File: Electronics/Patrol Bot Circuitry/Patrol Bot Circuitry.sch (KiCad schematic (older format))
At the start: 40 parts, among them J1 Left_Motor, J2 Right_Motor, J3 Battery, J4 AC_DC_10V, J5 Servo Motor, Q1 IRF4905, Q2 IRF4905, Q3 IRF4905, Q4 IRLZ44N, U1 ROB-14450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

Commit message: CAD Upload 1
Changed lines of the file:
@@
 U 1 1 619EC2A4
 P 3450 2100
-F 0 "U3" H 3650 1800 50  0000 C CNN
+F 0 "U3" H 3700 1800 50  0000 C CNN
 F 1 "MP1584EN" H 3400 1800 50  0000 C CNN
 F 2 "MP1584EN:MP1584EN" H 3450 2100 50  0001 C CNN

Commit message: Software Upload 1
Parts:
- removed C1: 0.1u, Capacitor_THT:CP_Axial_L10.0mm_D4.5mm_P15.00mm_Horizontal, symbol Device:C
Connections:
- net 3.3V: now also U1.2 (VCC)
- net 5V: no longer U1.2 (VCC)
- net IO1: now also U1.13 (STBY); no longer U11.8 (INT)
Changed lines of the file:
@@
-	1    0    0    -1
-$EndComp
-$Comp
-L HC-SR04:HC-SR04 U8
-U 1 1 61A3787B
-P 8300 4000
-F 0 "U8" H 8300 4200 50  0000 L CNN
-F 1 "HC-SR04" H 8450 4200 50  0000 L CNN
-F 2 "Connector_PinHeader_2.54mm:PinHeader_1x04_P2.54mm_Vertical" H 8300 4000 50  0001 L BNN
-F 3 "" H 8300 4000 50  0001 L BNN
-F 4 "Osepp" H 8300 4000 50  0001 L BNN "MANUFACTURER"
-	1    8300 4000
 	1    0    0    -1
 $EndComp
@@
 Wire Wire Line
 	5150 4150 5150 4250
-$Comp
-L Device:D_Photo D1
-U 1 1 61A649FF
-P 1450 6750
-F 0 "D1" V 1450 7050 50  0000 C CNN
-F 1 "D_Photo" V 1350 7050 50  0000 C CNN
-F 2 "OptoDevice:R_LDR_4.9x4.2mm_P2.54mm_Vertical" H 1400 6750 50  0001 C CNN
-F 3 "~" H 1400 6750 50  0001 C CNN
-	1    1450 6750
-	0    -1   -1   0
-$EndComp
 Text Notes 2000 7550 0    50   ~ 0
 Connect ADDR to \nGND for address 0x48.
@@
 	-1   0    0    -1
 $EndComp
-NoConn ~ 2700 4000
 $Comp
 L Connector:Screw_Terminal_01x02 J1
@@
 Wire Wire Line
 	6350 3350 6500 3350
-Wire Wire Line
-	6500 3350 6500 3900
-Wire Wire Line
-	6500 3900 8100 3900
 Wire Wire Line
 	6550 4100 8100 4100
@@
 Text Label 4450 4250 0    50   ~ 0
 IO1
-Text Label 9450 1700 0    50   ~ 0
-IO1
 Text Notes 8350 3100 0    50   ~ 0
 Must initialize IO1 \npin as interrupt.\n
@@
 Wire Wire Line
 	4050 6150 4200 6150
-$Comp
-L Device:C C1
-U 1 1 61C1ABD0
-P 1050 7100
-F 0 "C1" H 850 7100 50  0000 L CNN
-F 1 "0.1u" H 850 7000 50  0000 L CNN
-F 2 "Capacitor_THT:CP_Axial_L10.0mm_D4.5mm_P15.00mm_Horizontal" H 1088 6950 50  0001 C CNN
-F 3 "~" H 1050 7100 50  0001 C CNN
-	1    1050 7100
-	1    0    0    -1
-$EndComp
-Wire Wire Line
-	1050 6950 1450 6950
-Wire Wire Line
-	1050 7250 1450 7250
 NoConn ~ 4450 4050
 Wire Wire Line
@@
 Text Label 4850 6150 0    50   ~ 0
 3.3V
-Text Label 1450 6600 2    50   ~ 0
-3.3V
-Wire Wire Line
-	1450 6650 1450 6600
 Text Label 5950 2000 0    50   ~ 0
 5V
-Text Label 1500 3750 2    50   ~ 0
-5V
 Text Label 3250 3650 2    50   ~ 0
-5V
-Text Label 6500 3350 2    50   ~ 0
 5V
 Text Label 8100 4550 2    50   ~ 0
@@
 Battery
 NoConn ~ 3250 3750
+$Comp
+L HC-SR04:HC-SR04 U8
+U 1 1 61A3787B
+P 8300 4000
+F 0 "U8" H 8300 4200 50  0000 L CNN
+F 1 "HC-SR04" H 8450 4200 50  0000 L CNN
+F 2 "Connector_PinHeader_2.54mm:PinHeader_1x04_P2.54mm_Vertical" H 8300 4000 50  0001 L BNN
+F 3 "" H 8300 4000 50  0001 L BNN
+F 4 "Osepp" H 8300 4000 50  0001 L BNN "MANUFACTURER"
+	1    8300 4000
+	1    0    0    -1
+$EndComp
+Text Label 1500 3750 2    50   ~ 0
+3.3V
+NoConn ~ 9450 1700
+Text Label 2700 4000 0    50   ~ 0
+IO1
+Text Label 6500 3350 2    50   ~ 0
+5V
+Wire Wire Line
+	6500 3350 6500 3900
+Wire Wire Line
+	6500 3900 8100 3900
+Wire Wire Line
+	1450 6650 1450 6600
+Text Label 1450 6600 2    50   ~ 0
+3.3V
+$Comp
+L Device:D_Photo D1
+U 1 1 61A649FF
+P 1450 6750
+F 0 "D1" V 1500 6700 50  0000 C CNN
+F 1 "D_Photo" V 1500 7050 50  0000 C CNN
+F 2 "OptoDevice:R_LDR_4.9x4.2mm_P2.54mm_Vertical" H 1400 6750 50  0001 C CNN
+F 3 "~" H 1400 6750 50  0001 C CNN
+	1    1450 6750
+	0    -1   -1   0
+$EndComp
 $EndSCHEMATC

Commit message: Validation 1
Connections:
- net GND: now also U11.7 (AD0)
- no-connect marks 29 -> 28
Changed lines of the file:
@@
 NoConn ~ 8250 2500
 NoConn ~ 8250 2000
-NoConn ~ 8250 1700
 NoConn ~ 8250 1600
 NoConn ~ 8250 1500
@@
 	0    -1   -1   0
 $EndComp
+$Comp
+L power:GND #PWR?
+U 1 1 61CAC55A
+P 8250 1700
+F 0 "#PWR?" H 8250 1450 50  0001 C CNN
+F 1 "GND" H 8255 1527 50  0000 C CNN
+F 2 "" H 8250 1700 50  0001 C CNN
+F 3 "" H 8250 1700 50  0001 C CNN
+	1    8250 1700
+	1    0    0    -1
+$EndComp
 $EndSCHEMATC

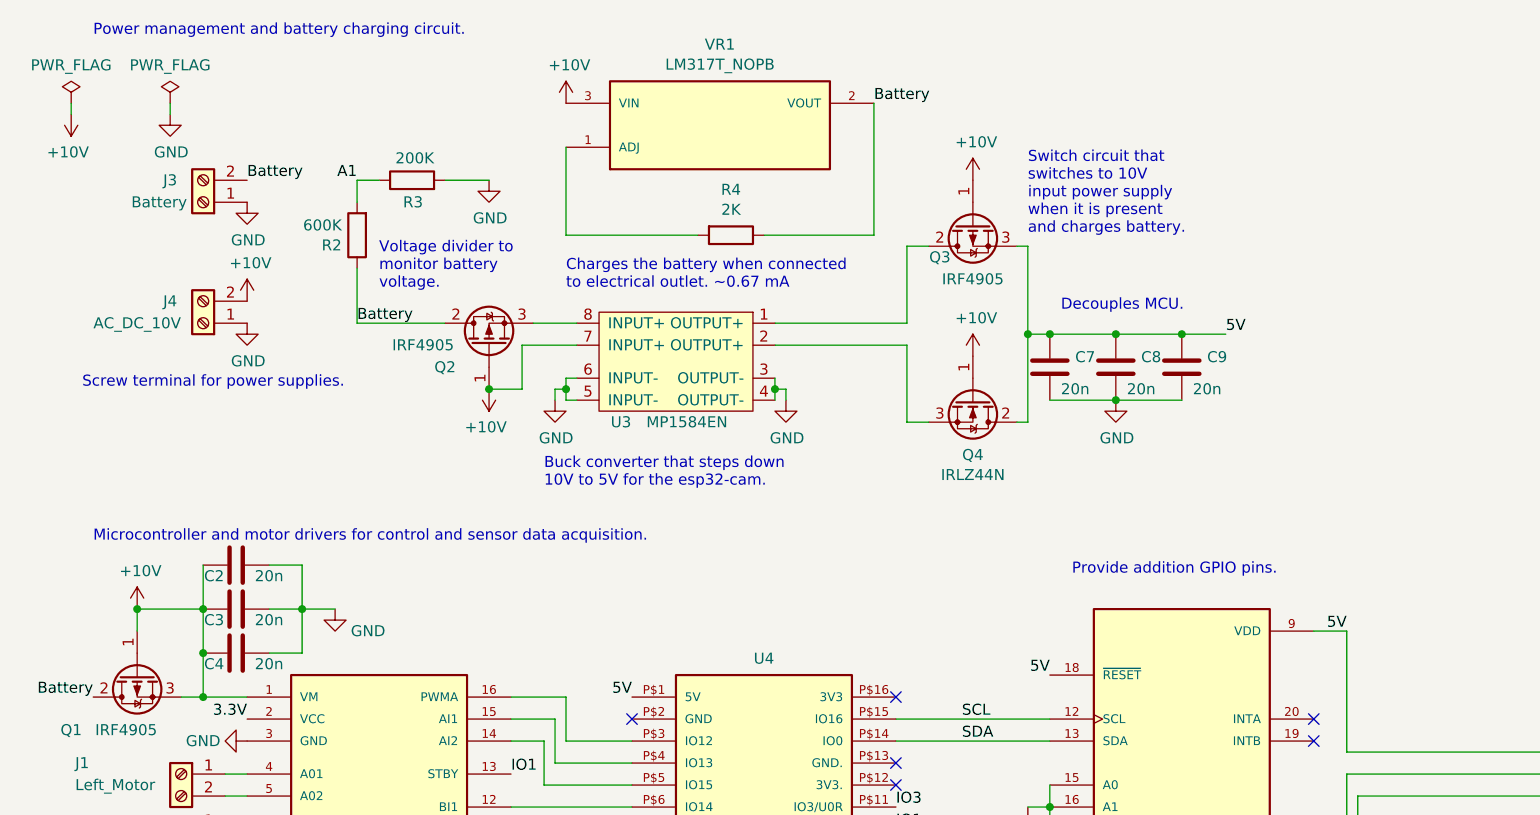
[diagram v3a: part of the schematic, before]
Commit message: Fixed Power Management Switches
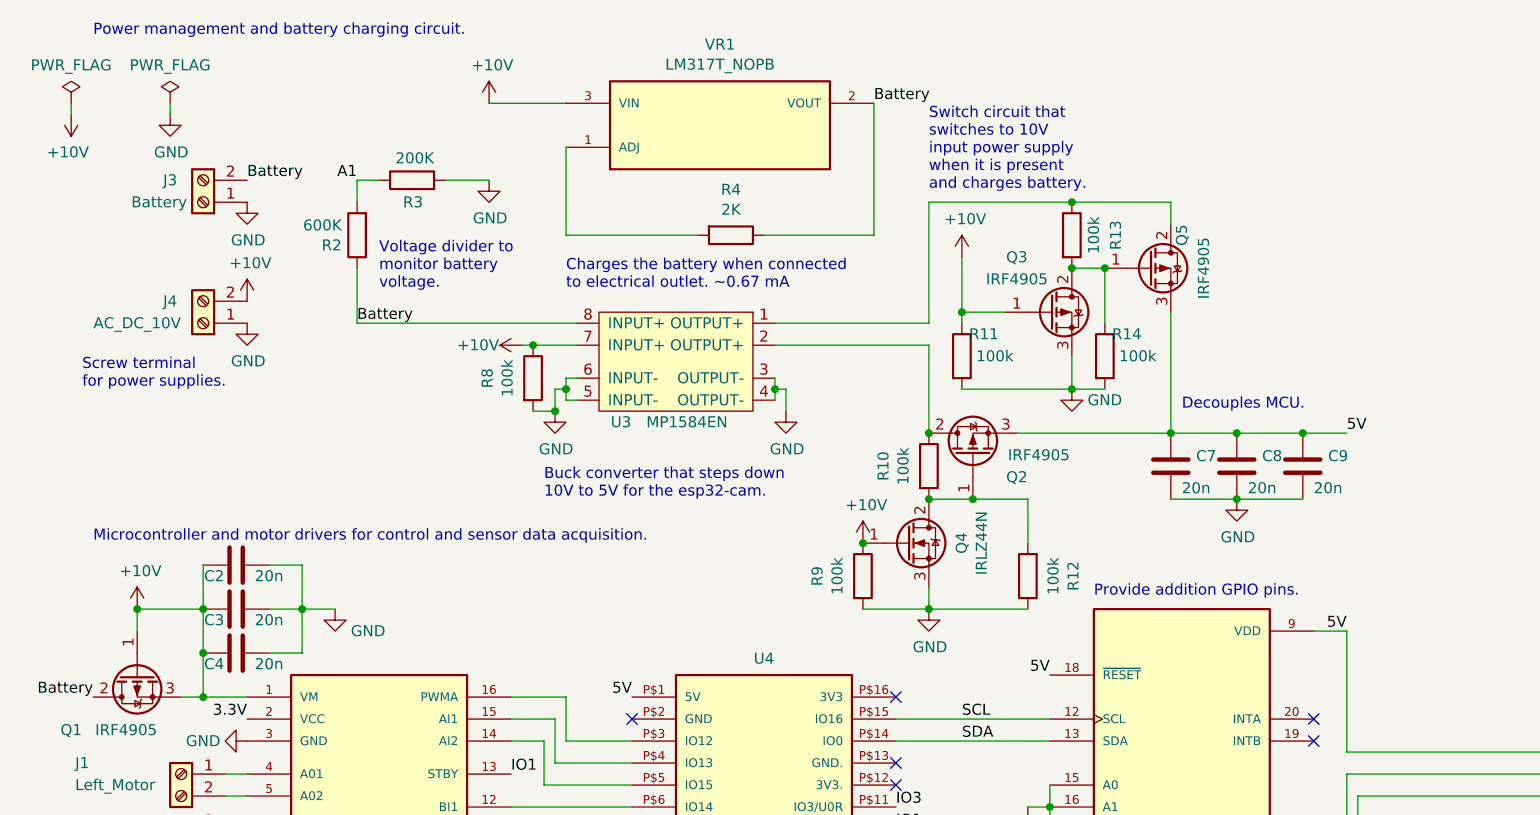
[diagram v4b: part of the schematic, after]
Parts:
- added Q5: IRF4905, Package_TO_SOT_THT:TO-220-3_Vertical, symbol Transistor_FET:IRF4905
- added R10, R11, R12, R13, R14, R8, R9: 100k, Resistor_THT:R_Axial_DIN0204_L3.6mm_D1.6mm_P1.90mm_Vertical, symbol Device:R
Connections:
- net +10V: now also R11.1, R8.1, R9.1; no longer Q2.1 (G)
- net 5V: now also Q2.3 (S), Q5.3 (S); no longer Q3.3 (S), Q4.2 (D)
- net Battery: now also U3.8 (INPUT+); no longer Q2.2 (D)
- net GND: now also Q3.3 (S), Q4.3 (S), R11.2, R12.1, R14.2, R8.2, R9.2
- net at U3.1 (OUTPUT+): now also Q5.2 (D), R13.1; no longer Q3.2 (D)
- net at U3.2 (OUTPUT+): now also Q2.2 (D), R10.1; no longer Q4.3 (S)
- new net: Q2.1 (G), Q4.2 (D), R10.2, R12.2
- new net: Q3.2 (D), Q5.1 (G), R13.2, R14.1
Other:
- note added: "Screw terminal \nfor power supplies."
- note removed: "Screw terminal for power supplies."
- moved on the sheet: C7, C8, C9, Q4

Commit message: Redesigned PCB / Mechanical Drawing
ESP32-cam not connecting to Wifi -> must DEBUG
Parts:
- removed Q1, Q2, Q3, Q5: IRF4905, Package_TO_SOT_THT:TO-220-3_Vertical, symbol Transistor_FET:IRF4905
- removed Q4: IRLZ44N, Package_TO_SOT_THT:TO-220-3_Vertical, symbol Transistor_FET:IRLZ44N
- removed R14: 100k, Resistor_THT:R_Axial_DIN0204_L3.6mm_D1.6mm_P1.90mm_Vertical, symbol Device:R
- removed R5: 30, Resistor_THT:R_Axial_DIN0204_L3.6mm_D1.6mm_P1.90mm_Vertical, symbol Device:R
- removed U7: MCP23017-E_SP, MCP23017:DIP787W45P254L3556H508Q28, symbol MCP23017-E_SP:MCP23017-E_SP
- added C1: 0.47u, Capacitor_SMD:C_0603_1608Metric, symbol Device:C
- added Q1, Q3: Q_NMOS_GSD, Package_TO_SOT_SMD:SOT-23, symbol Device:Q_NMOS_GSD
- added Q2, Q4, Q5: Q_PMOS_GSD, Package_TO_SOT_SMD:SOT-23, symbol Device:Q_PMOS_GSD
- added U7: PCF8574, PCF8574N:DIP794W45P254L1969H508Q16, symbol Interface_Expansion:PCF8574
- C2: value 20n -> 0.01n; footprint Capacitor_THT:CP_Axial_L10.0mm_D4.5mm_P15.00mm_Horizontal -> Capacitor_SMD:C_0603_1608Metric
- C3, C8: value 20n -> 0.1u; footprint Capacitor_THT:CP_Axial_L10.0mm_D4.5mm_P15.00mm_Horizontal -> Capacitor_SMD:C_0603_1608Metric
- C4, C7: value 20n -> 0.47u; footprint Capacitor_THT:CP_Axial_L10.0mm_D4.5mm_P15.00mm_Horizontal -> Capacitor_SMD:C_0603_1608Metric
- C5, C6: footprint Capacitor_THT:CP_Axial_L10.0mm_D4.5mm_P15.00mm_Horizontal -> Capacitor_THT:CP_Radial_D7.5mm_P2.50mm
- C9: value 20n -> 0.01u; footprint Capacitor_THT:CP_Axial_L10.0mm_D4.5mm_P15.00mm_Horizontal -> Capacitor_SMD:C_0603_1608Metric
- D2, D3: footprint LED_THT:LED_D1.8mm_W3.3mm_H2.4mm -> LED_THT:LED_D3.0mm
- R1: value 100K -> 200K; footprint Resistor_THT:R_Axial_DIN0204_L3.6mm_D1.6mm_P1.90mm_Vertical -> Resistor_SMD:R_0603_1608Metric
- R10, R11, R12, R13, R8, R9: value 100k -> 200k; footprint Resistor_THT:R_Axial_DIN0204_L3.6mm_D1.6mm_P1.90mm_Vertical -> Resistor_SMD:R_0603_1608Metric
- R2: value 600K -> 620K; footprint Resistor_THT:R_Axial_DIN0204_L3.6mm_D1.6mm_P1.90mm_Vertical -> Resistor_SMD:R_0603_1608Metric
- R3, R4, R6, R7: footprint Resistor_THT:R_Axial_DIN0204_L3.6mm_D1.6mm_P1.90mm_Vertical -> Resistor_SMD:R_0603_1608Metric
- U11: footprint MPU-6050:QFN50P400X400X95-24N -> Connector_PinSocket_2.54mm:PinSocket_1x08_P2.54mm_Vertical
- U2: footprint ADS1115:ADS1115 -> Connector_PinSocket_2.54mm:PinSocket_1x10_P2.54mm_Vertical
- U6: footprint MAX9814:MAX9814 -> Connector_PinSocket_2.54mm:PinSocket_1x05_P2.54mm_Vertical
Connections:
- net 5V is gone; now on net +5V: C7.1, C8.1, C9.1, J5.2 (Pin_2), U10.1 (VCC), U2.1 (VDD), U4.P$1 (5V), U8.1 (VCC), U9.1 (VCC)
- net +10V: now also Q1.1 (G), Q3.1 (G); no longer C2.2, C3.2, C4.2, U1.1 (VM)
- net A1: now also C1.2
- net Battery: now also C2.2, C3.2, C4.2, U1.1 (VM)
- net GND: now also R12.2, C1.1, Q1.2 (S), Q3.2 (S), U7.1 (A0), U7.2 (A1), U7.3 (A2), U7.8 (VSS); no longer R12.1
- net SCL: now also U7.14 (SCL)
- net SDA: now also U7.15 (SDA)
- net at R13.1, U3.1 (OUTPUT+): now also Q4.2 (S), Q5.2 (S)
- net at R10.1, U3.2 (OUTPUT+): now also Q2.2 (S)
- net at U8.2 (TRIG): now also U7.4 (P0)
- net at U8.3 (ECHO): now also U7.5 (P1)
- net at U9.2 (TRIG): now also U7.6 (P2)
- net at U9.3 (ECHO): now also U7.7 (P3)
- net at R6.2: now also U7.9 (P4)
- net at R7.2: now also U7.10 (P5)
- net at U10.2 (TRIG): now also U7.11 (P6)
- net at U10.3 (ECHO): now also U7.12 (P7)
- net at R10.2: now also Q1.3 (D), Q2.1 (G); no longer R12.2
- net +5V: now reaches C5.1, U5.1 (VI)
- net +5V: now also Q2.3 (D), Q5.3 (D), U7.16 (VDD)
- net at R13.2: now also Q3.3 (D), Q4.1 (G)
- new net: Q4.3 (D), Q5.1 (G), R12.1
- no-connect marks 28 -> 11
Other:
- note added: "IO Expander\n"
- note added: "Microcontroller and motor drivers for \ncontrol and sensor data acquisition."
- note removed: "Microcontroller and motor drivers for control and sensor data acquisition."
- note removed: "Provide addition GPIO pins."
- moved on the sheet: C7, C8, J3, J4
